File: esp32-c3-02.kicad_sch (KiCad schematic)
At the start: 0 parts

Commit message: 1.2.0 Schematic design page 2
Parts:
- added J3: GSD090012SEU, GSD090012SEU:AMPHENOL_GSD090012SEU, symbol GSD090012SEU:GSD090012SEU
- added U3: ESP32-C3-WROOM-02-H4, ESP32-C3-WROOM-02-H4:MODULE_ESP32-C3-WROOM-02-H4, symbol ESP32-C3-WROOM-02-H4:ESP32-C3-WROOM-02-H4
- added U4: CP2102N-Axx-xQFN20, Package_DFN_QFN:SiliconLabs_QFN-20-1EP_3x3mm_P0.5mm, symbol Interface_USB:CP2102N-Axx-xQFN20
- added U5: USBLC6-2SC6, Package_TO_SOT_SMD:SOT-23-6, symbol Power_Protection:USBLC6-2SC6
- added U6: W25Q32JVSSIQ, W25Q32JVSSIQ:SOIC127P790X216-8N, symbol W25Q32JVSSIQ:W25Q32JVSSIQ
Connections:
- new net: U4.12 (GND), U4.21 (GND), U4.3 (GND)
- new net GND: U3.19 (GND), U3.20 (GND), U3.21 (GND), U3.22 (GND), U3.23 (GND), U3.24 (GND), U3.25 (GND), U3.26 (GND), U3.27 (GND), U3.28 (GND), U3.29 (GND), U3.30 (GND), U3.31 (GND), U3.32 (GND), U3.33 (GND), U3.34 (GND), U3.35 (GND), U3.36 (GND), U3.37 (GND), U3.38 (GND), U3.39 (GND), U3.9 (GND)
- new net SHIELD_GND: J3.G1 (SHIELD_GND), J3.G2 (SHIELD_GND), J3.G3 (SHIELD_GND), J3.G4 (SHIELD_GND)

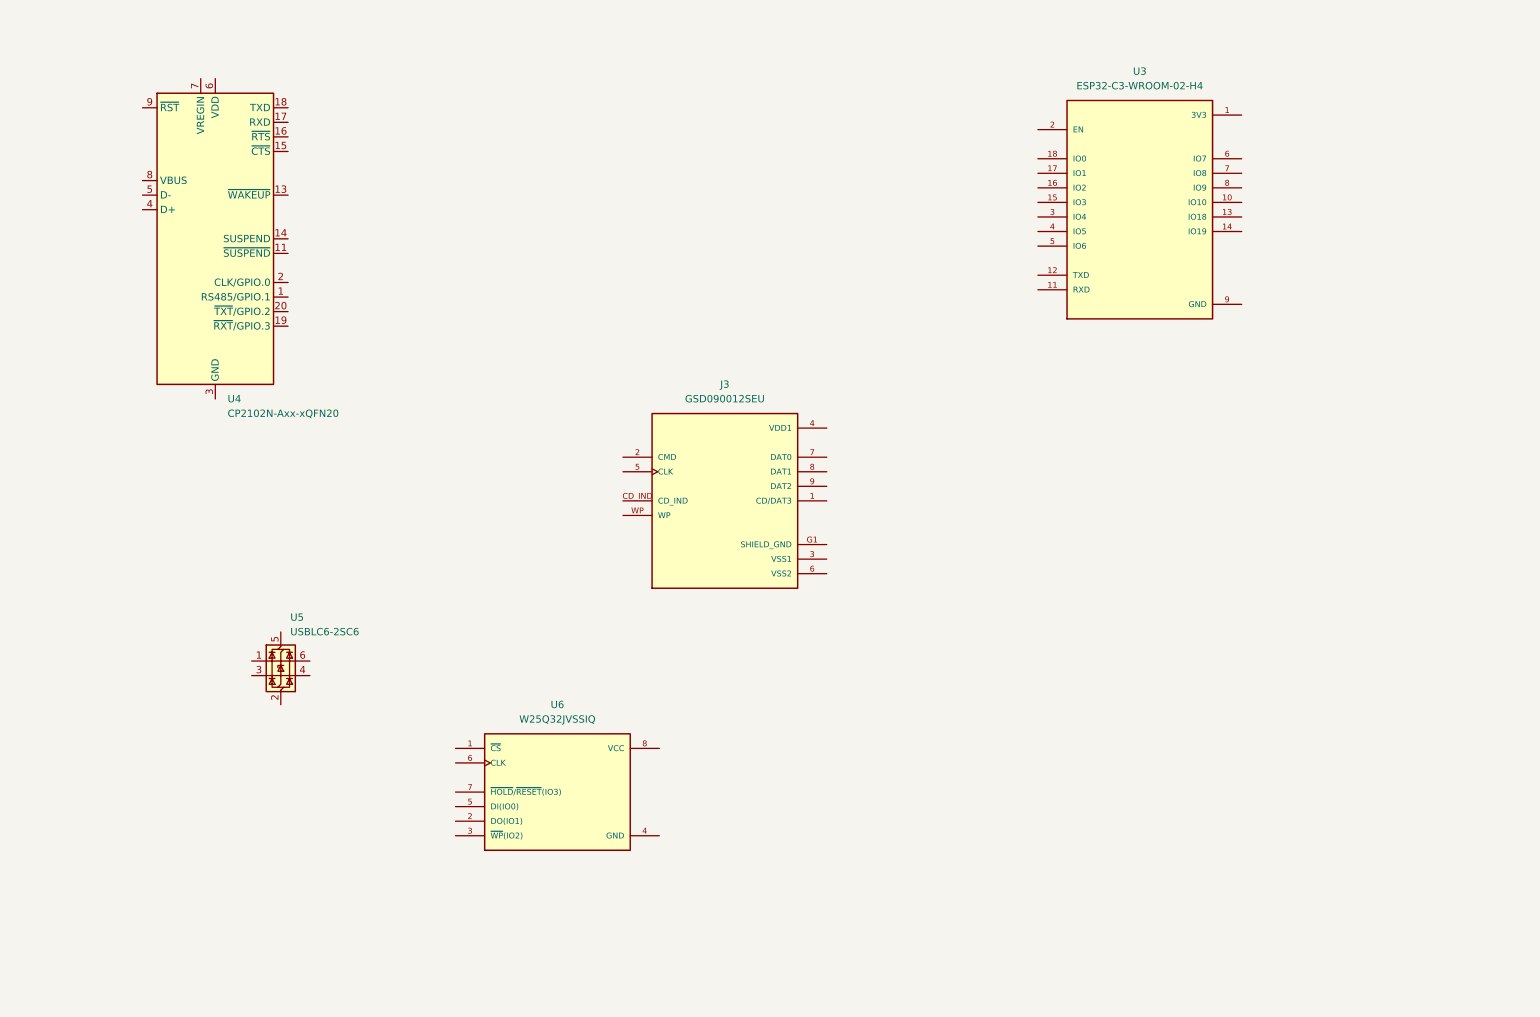
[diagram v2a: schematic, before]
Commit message: 1.2.1 Design the USB to UART bridge subcircuit
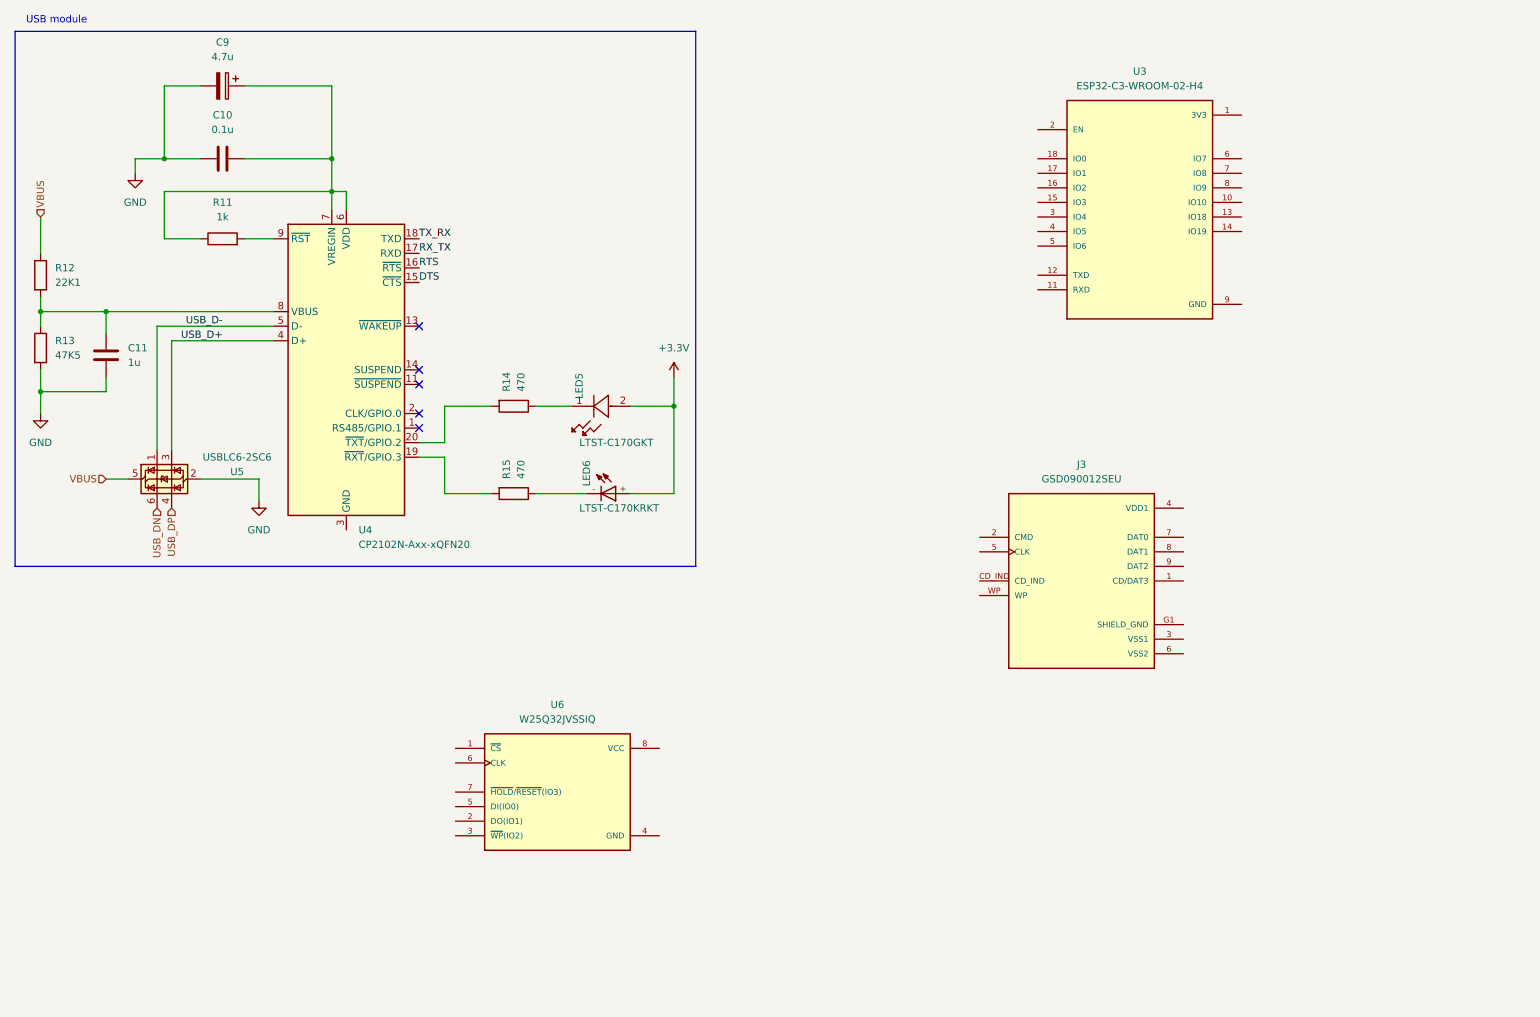
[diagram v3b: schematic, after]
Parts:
- added C10: 0.1u, symbol Device:C
- added C11: 1u, symbol Device:C
- added C9: 4.7u, symbol Device:C_Polarized
- added LED5: LTST-C170GKT, LED_LTST-C170GKT_LTO, symbol LTST-C170GKT:LTST-C170GKT
- added LED6: LTST-C170KRKT, LTST-C170KRKT:DIOC200X125X110, symbol LTST-C170KRKT:LTST-C170KRKT
- added R11: 1k, symbol Device:R
- added R12: 22K1, symbol Device:R
- added R13: 47K5, symbol Device:R
- added R14, R15: 470, symbol Device:R
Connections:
- net GND: now also U5.2 (GND), C10.1, C11.2, C9.2, R13.2
- net DTS: now reaches U4.15 (~{CTS})
- net RTS: now reaches U4.16 (~{RTS})
- net RX_TX: now reaches U4.17 (RXD)
- net TX_RX: now reaches U4.18 (TXD)
- net at U4.19 (~{RXT}/GPIO.3): now also R15.2
- net at U4.20 (~{TXT}/GPIO.2): now also R14.2
- net USB_D+: now reaches U4.4 (D+)
- net USB_D+: now also U5.3 (I/O2)
- net USB_D-: now reaches U4.5 (D-)
- net USB_D-: now also U5.1 (I/O1)
- net at U4.6 (VDD): now also U4.7 (VREGIN), C10.2, C9.1, R11.1
- net at U4.8 (VBUS): now also C11.1, R12.2, R13.1
- net at U4.9 (~{RST}): now also R11.2
- net USB_DP: now reaches U5.4 (I/O2)
- net VBUS: now reaches U5.5 (VBUS)
- net VBUS: now also R12.1
- net USB_DN: now reaches U5.6 (I/O1)
- new net: LED6.-, R15.1
- new net: LED5.1, R14.1
- new net +3.3V: LED5.2, LED6.+
- no-connect marks 0 -> 5
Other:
- note added: "USB module"
- moved on the sheet: J3, U4, U5

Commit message: 1.2.2 Project Design the ESP32 module subcircuit
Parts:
- added C7: 10u, symbol Device:C_Polarized
- added C8: 0.1u, symbol Device:C
- added R15, R20: 50, symbol Device:R
- renumbered R15 to R18
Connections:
- net +3.3V: now also U3.1 (3V3), C7.1, C8.1
- net GND: now also C7.2, C8.2
- net RX_TX: now also U3.12 (TXD)
- net TX_RX: now also U3.11 (RXD)
- net CS: now reaches U3.10 (IO10)
- net GPIO18: now reaches U3.13 (IO18)
- net GPIO19: now reaches U3.14 (IO19)
- net SCL: now reaches U3.15 (IO3)
- net MISO_DO: now reaches U3.16 (IO2)
- net PHOTO_C: now reaches U3.17 (IO1)
- net CD_SD: now reaches U3.18 (IO0)
- net EN: now reaches U3.2 (EN)
- net SDA: now reaches U3.3 (IO4)
- net MIC_OUT: now reaches U3.4 (IO5)
- net at U3.5 (IO6): now also R20.2
- net at U3.6 (IO7): now also R15.1
- net GPIO8: now reaches U3.7 (IO8)
- net BOOT: now reaches U3.8 (IO9)
- new net MOSI_DI: R15.2
- new net SCLK: R20.1
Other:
- moved on the sheet: LED6

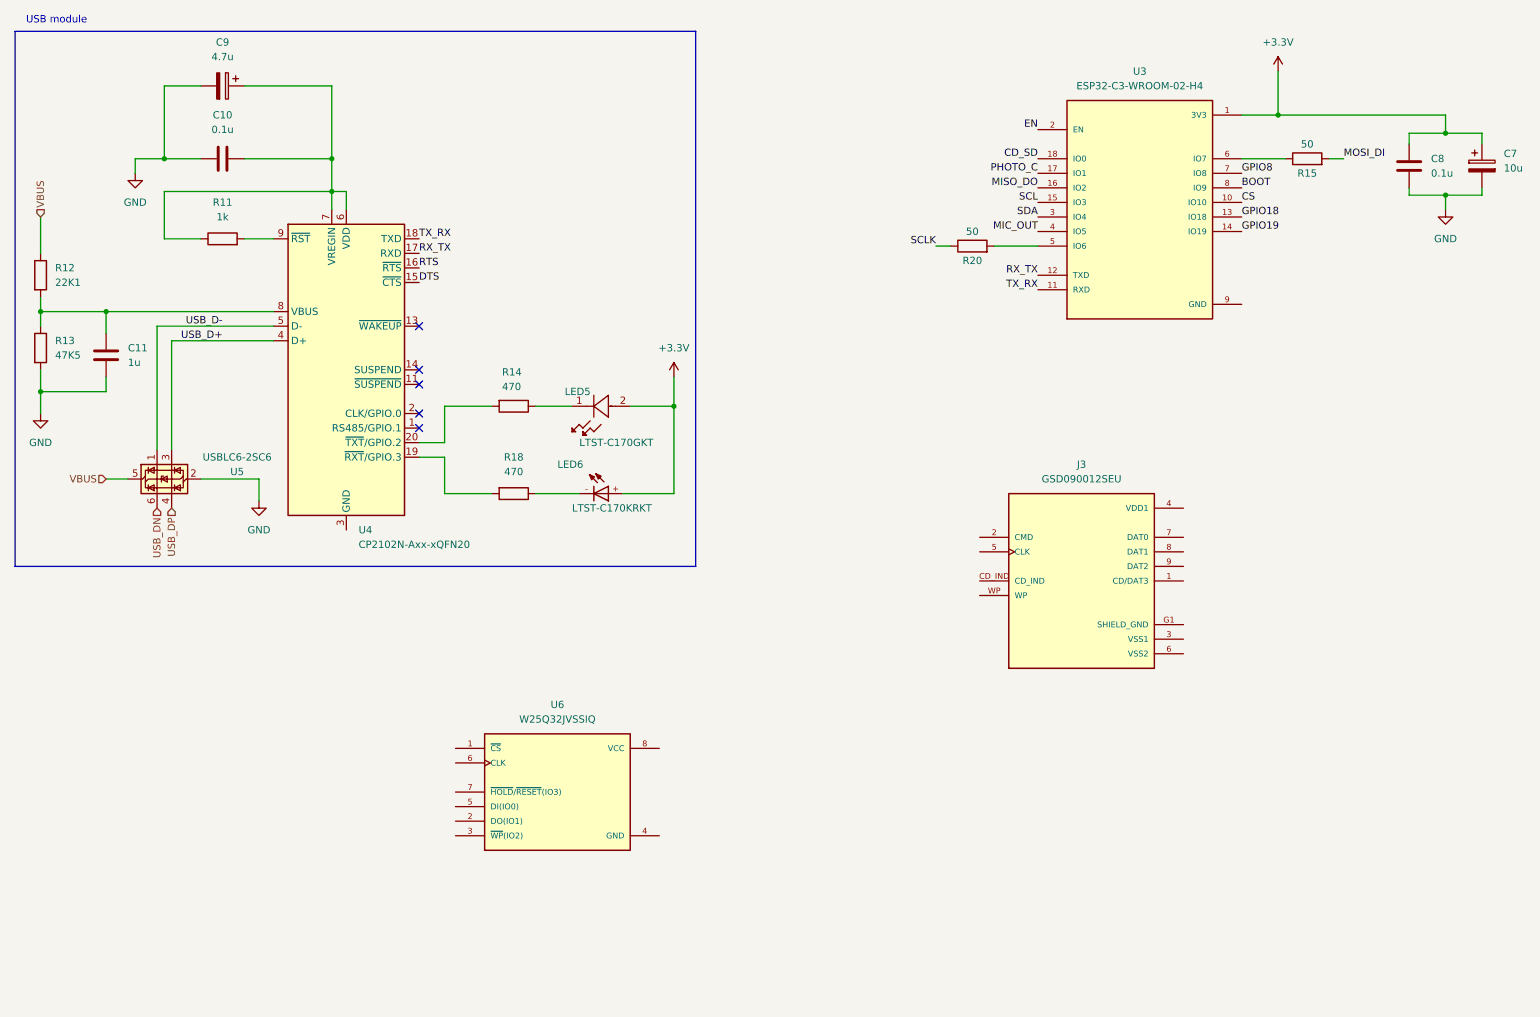
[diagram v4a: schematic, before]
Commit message: 1.2.3 Design the SD card module subcircuit
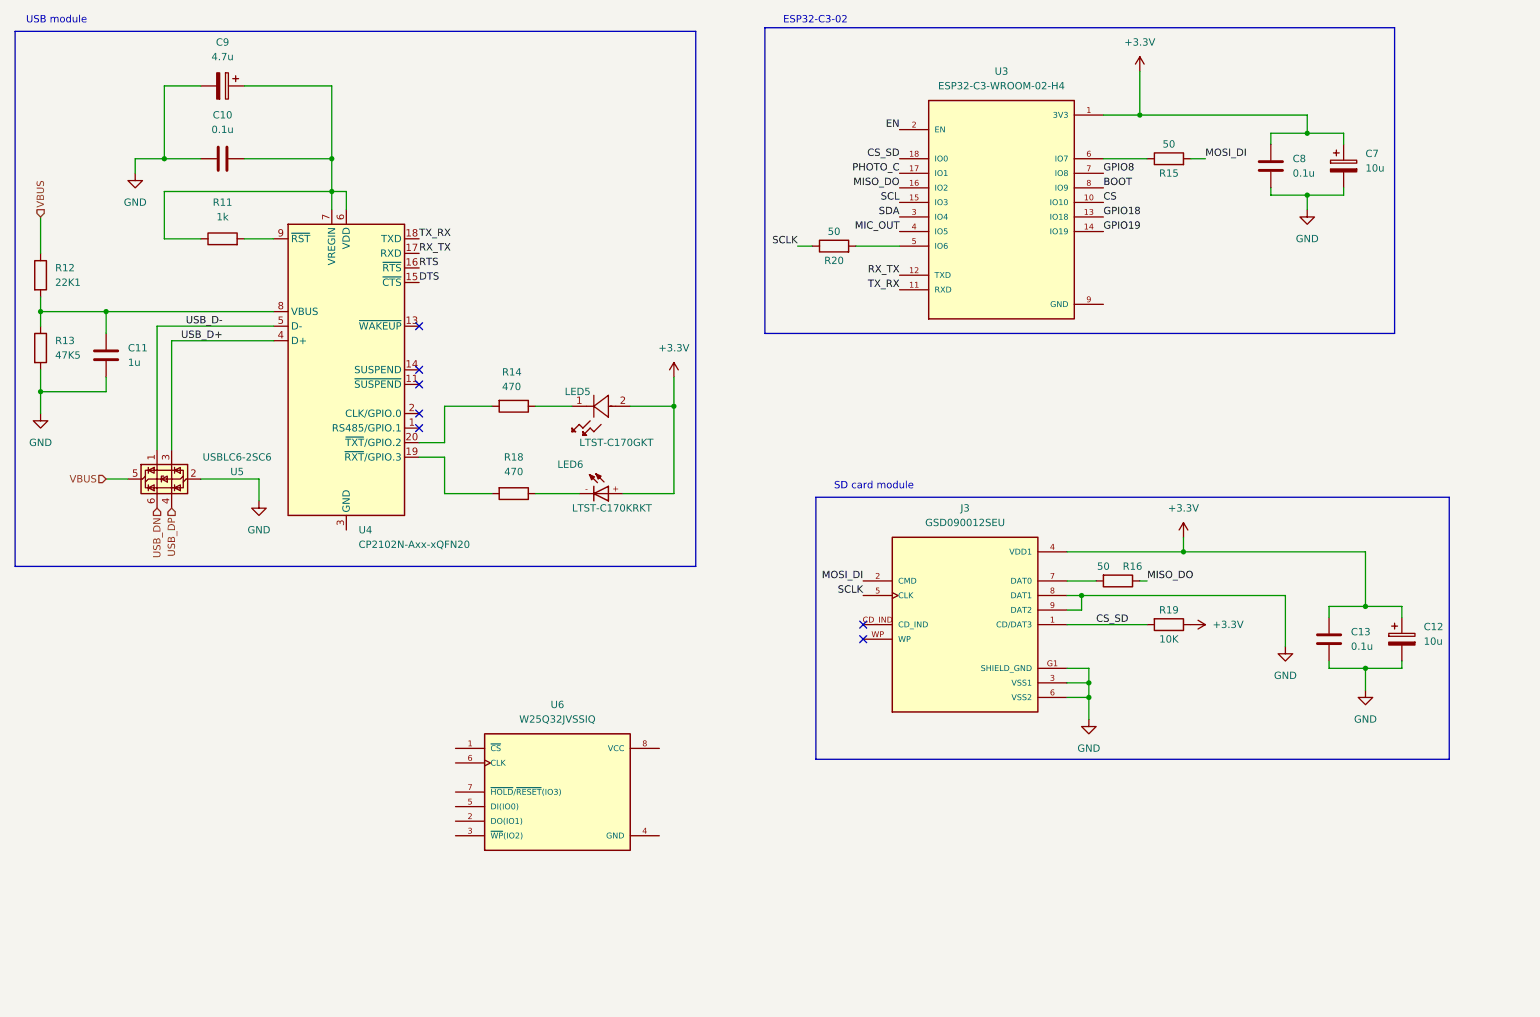
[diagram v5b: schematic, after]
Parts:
- added C12: 10u, symbol Device:C_Polarized
- added C13: 0.1u, symbol Device:C
- added R16: 50, symbol Device:R
- added R19: 10K, symbol Device:R
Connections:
- net CD_SD is gone; now on net CS_SD: U3.18 (IO0)
- net SHIELD_GND is gone; now on net GND: J3.G1 (SHIELD_GND), J3.G2 (SHIELD_GND), J3.G3 (SHIELD_GND), J3.G4 (SHIELD_GND)
- net +3.3V: now also J3.4 (VDD1), C12.1, C13.1, R19.1
- net GND: now also J3.3 (VSS1), J3.6 (VSS2), J3.8 (DAT1), J3.9 (DAT2), C12.2, C13.2
- net MISO_DO: now also R16.1
- net MOSI_DI: now also J3.2 (CMD)
- net SCLK: now also J3.5 (CLK)
- net CS_SD: now reaches J3.1 (CD/DAT3)
- net CS_SD: now also R19.2
- net at J3.7 (DAT0): now also R16.2
- no-connect marks 5 -> 7
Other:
- note added: "ESP32-C3-02"
- note added: "SD card module"
- moved on the sheet: C7, C8, J3, R15, R20, U3

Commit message: 1.2.4 Design the flash memory subcircuit
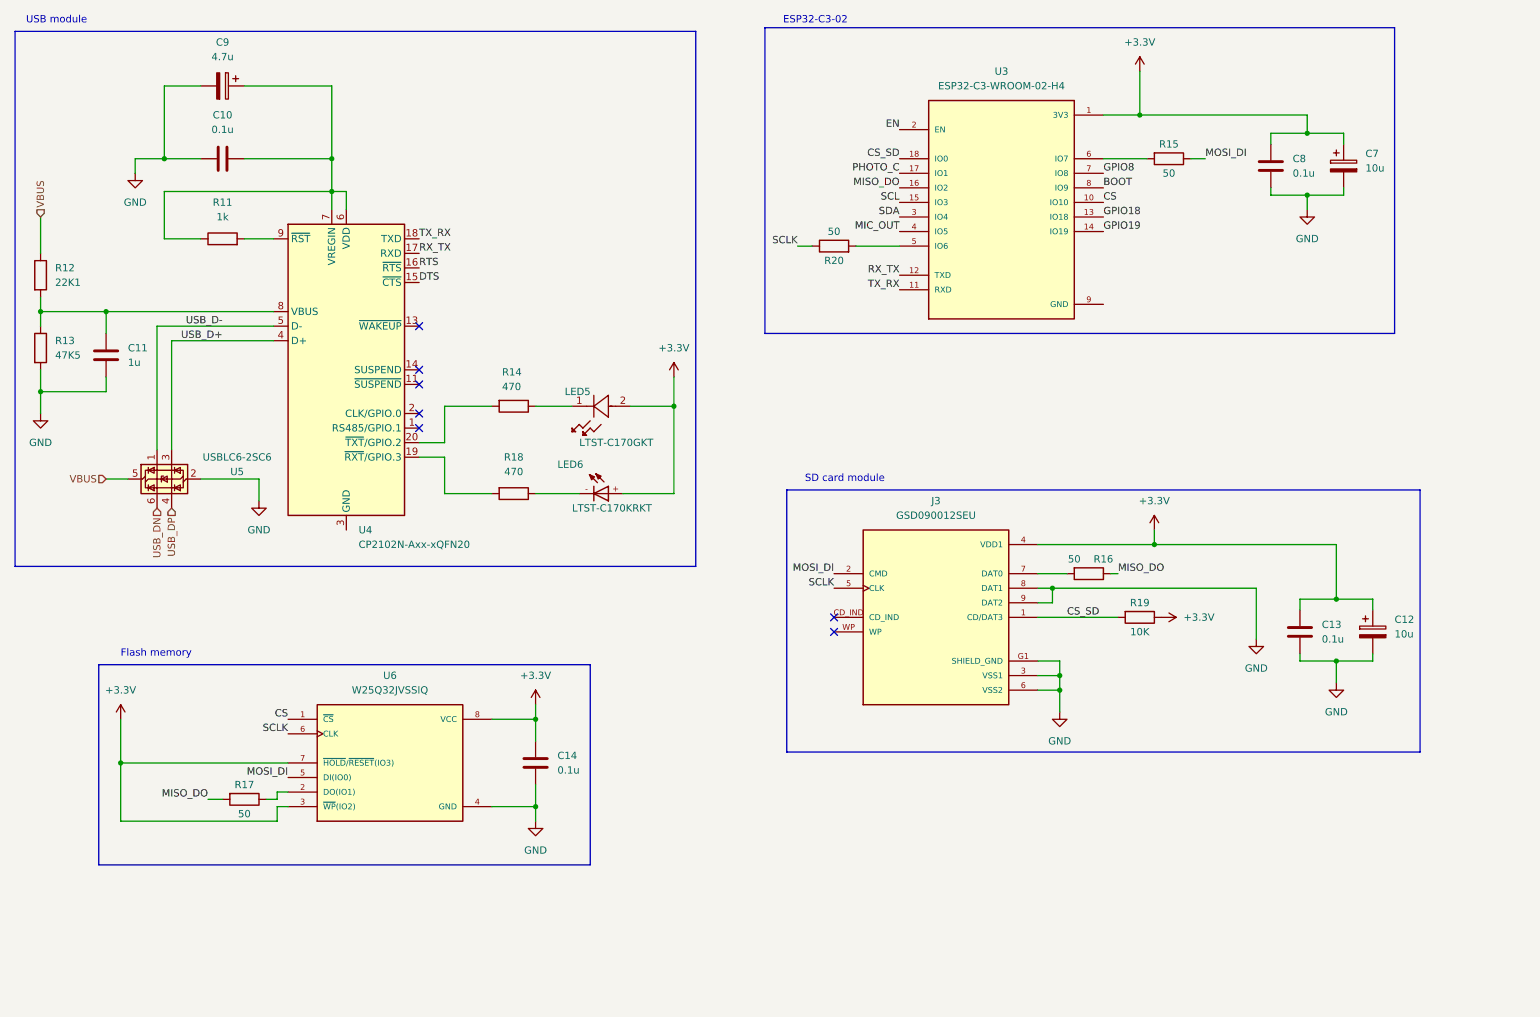
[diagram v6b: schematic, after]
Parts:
- added C14: 0.1u, symbol Device:C
- added R17: 50, symbol Device:R
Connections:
- net +3.3V: now also U6.3 (~{WP}(IO2)), U6.7 (~{HOLD}/~{RESET}(IO3)), U6.8 (VCC), C14.1
- net CS: now also U6.1 (~{CS})
- net GND: now also U6.4 (GND), C14.2
- net MISO_DO: now also R17.2
- net MOSI_DI: now also R15.1, U6.5 (DI(IO0)); no longer R15.2
- net SCLK: now also U6.6 (CLK)
- net at U6.2 (DO(IO1)): now also R17.1
- net at U3.6 (IO7): now also R15.2; no longer R15.1
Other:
- note added: "Flash memory"
- moved on the sheet: C12, C13, J3, R15, R16, R19, U6

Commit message: 1.2.5 Create hierarchical sheet 3 & 4 symbols
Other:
- added sheet Sensors (sensors.kicad_sch)
- added sheet User interface (user_interface.kicad_sch)
- company: (none) -> Nonexistent Co.
- title: (none) -> ESP32 C3, USB and flash memory
- moved on the sheet: C14, R17, U6
